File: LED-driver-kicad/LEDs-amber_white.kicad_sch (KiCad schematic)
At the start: 46 parts, among them Q3 2N7002K, Q7 Q_PMOS_GDS, Q8 Q_NMOS_GDS, U7 MIC3205YML-TR

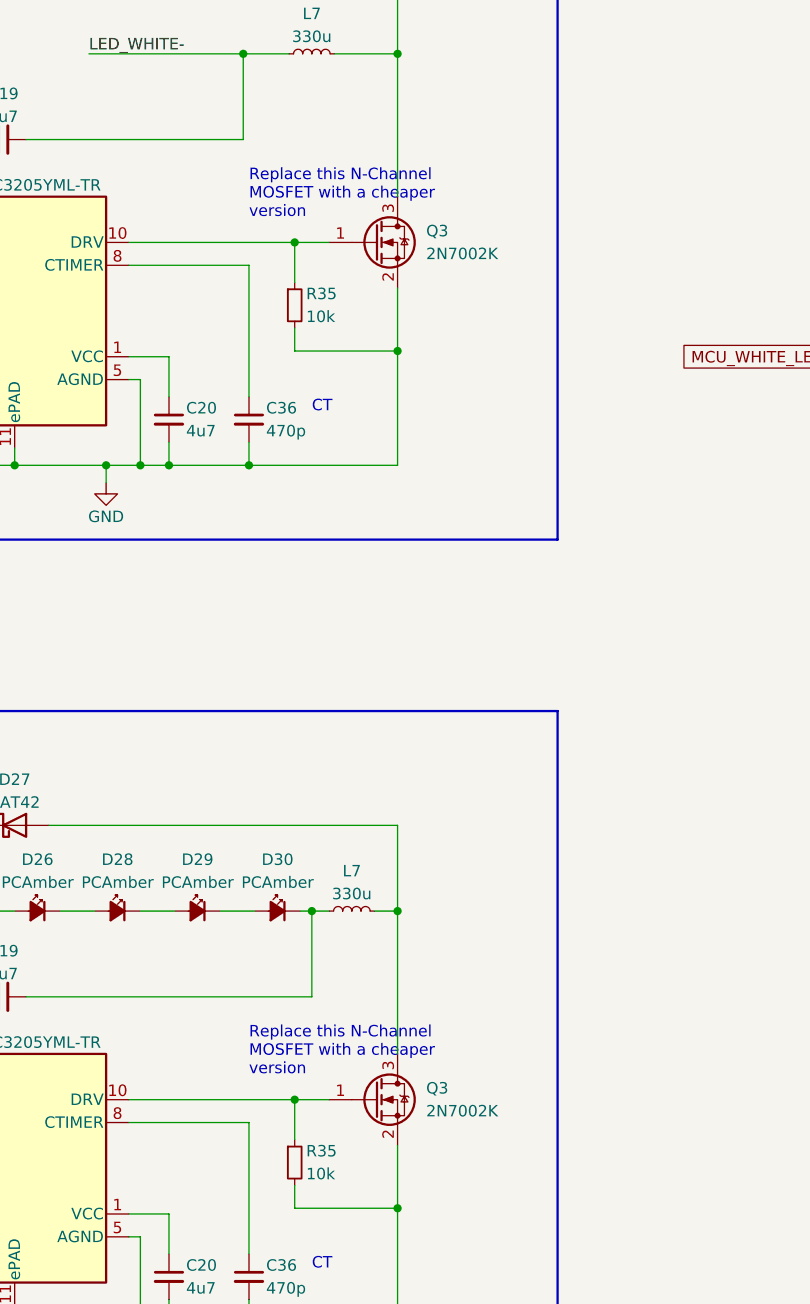
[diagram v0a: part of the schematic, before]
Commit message: replace MOSFETs with generic n-channel MSOFETs
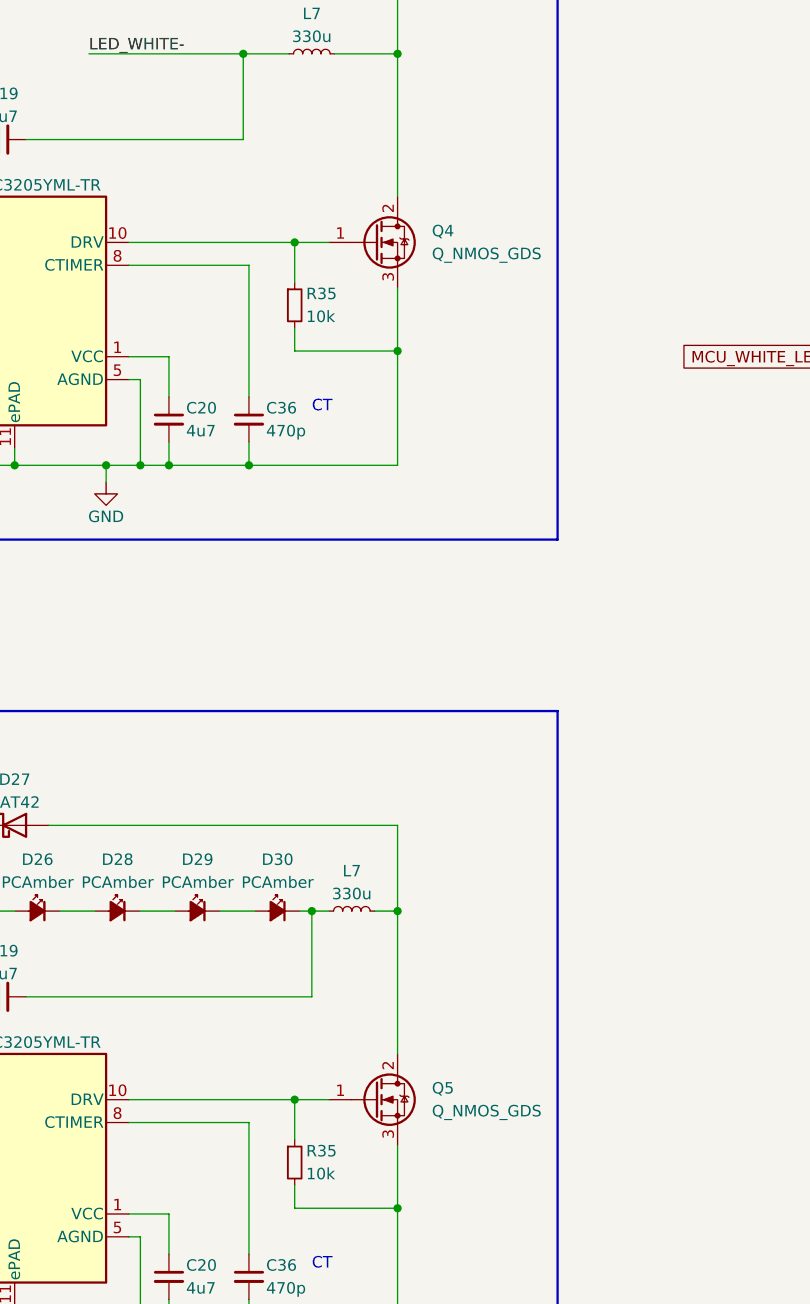
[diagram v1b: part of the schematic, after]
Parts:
- removed Q3 (x2): 2N7002K, Package_TO_SOT_SMD:SOT-23, symbol Transistor_FET:2N7002K
- added Q4, Q5: Q_NMOS_GDS, symbol Device:Q_NMOS_GDS
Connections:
- net GND: now also Q4.3 (S), Q5.3 (S)
- net at D27.2 (A), L7.2: now also Q4.2 (D)
- net at R35.1, U7.10 (DRV): now also Q5.1 (G)
- net at D27.2 (A), L7.2: now also Q5.2 (D)
- net at R35.1, U7.10 (DRV): now also Q4.1 (G)
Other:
- note removed: "Replace this N-Channel MOSFET with a cheaper version"

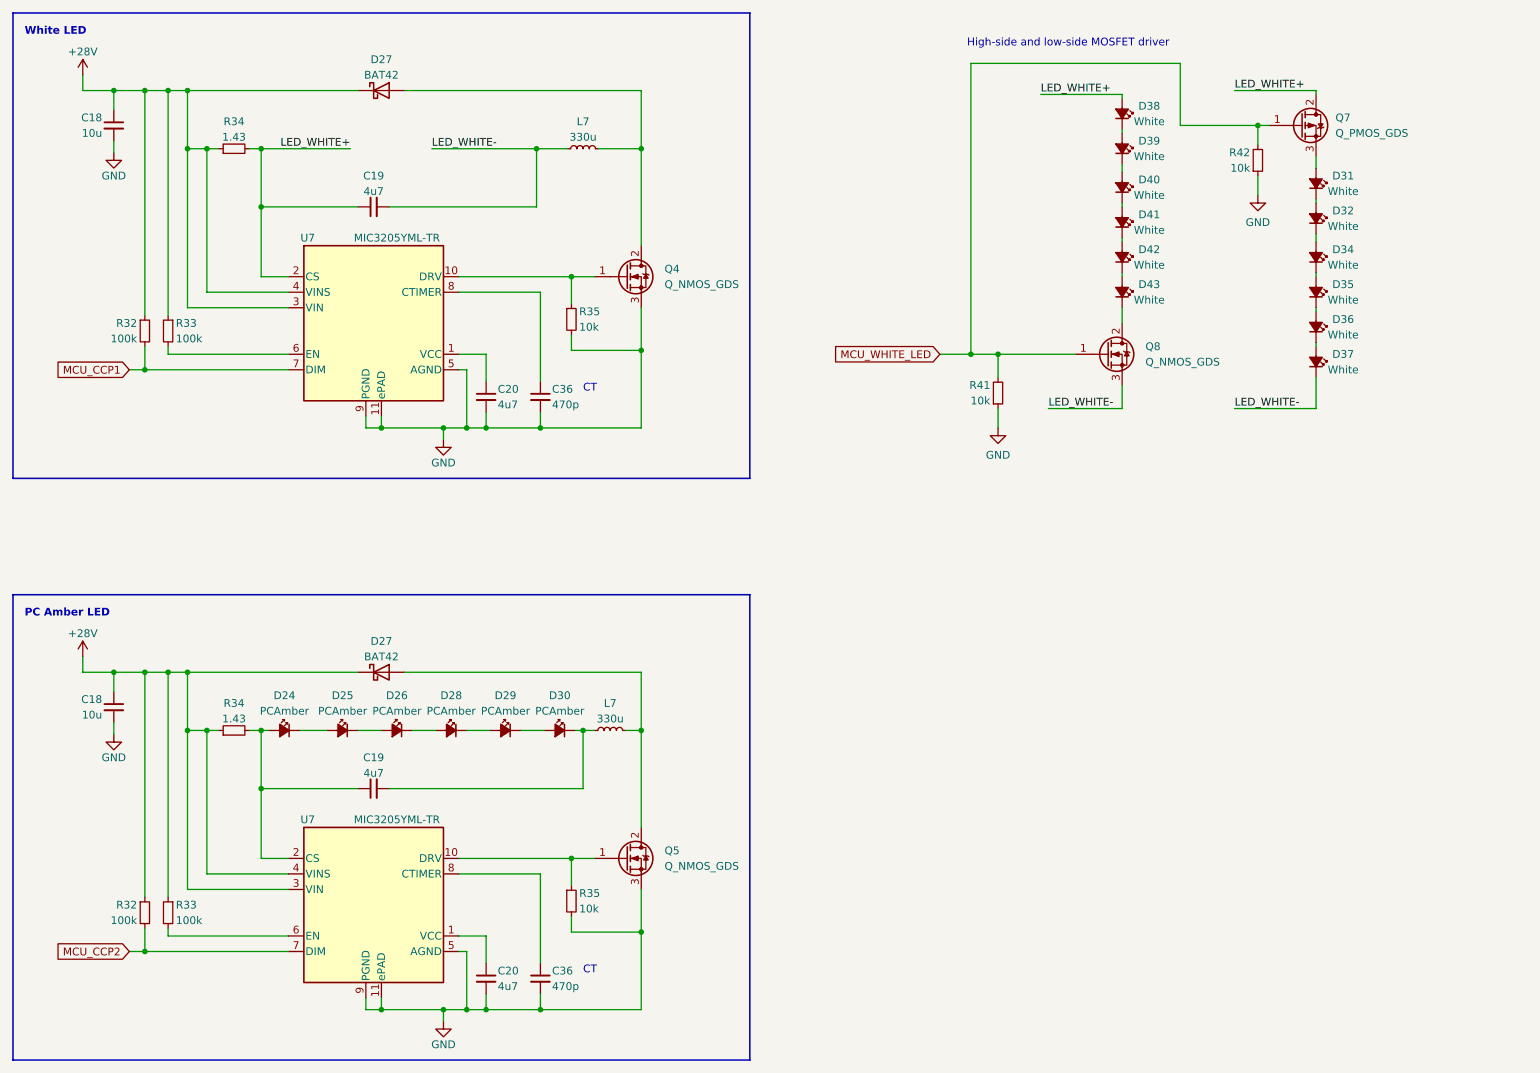
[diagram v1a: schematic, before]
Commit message: replace push-pull MOSFET circuit with LED driver with inverter gate enable
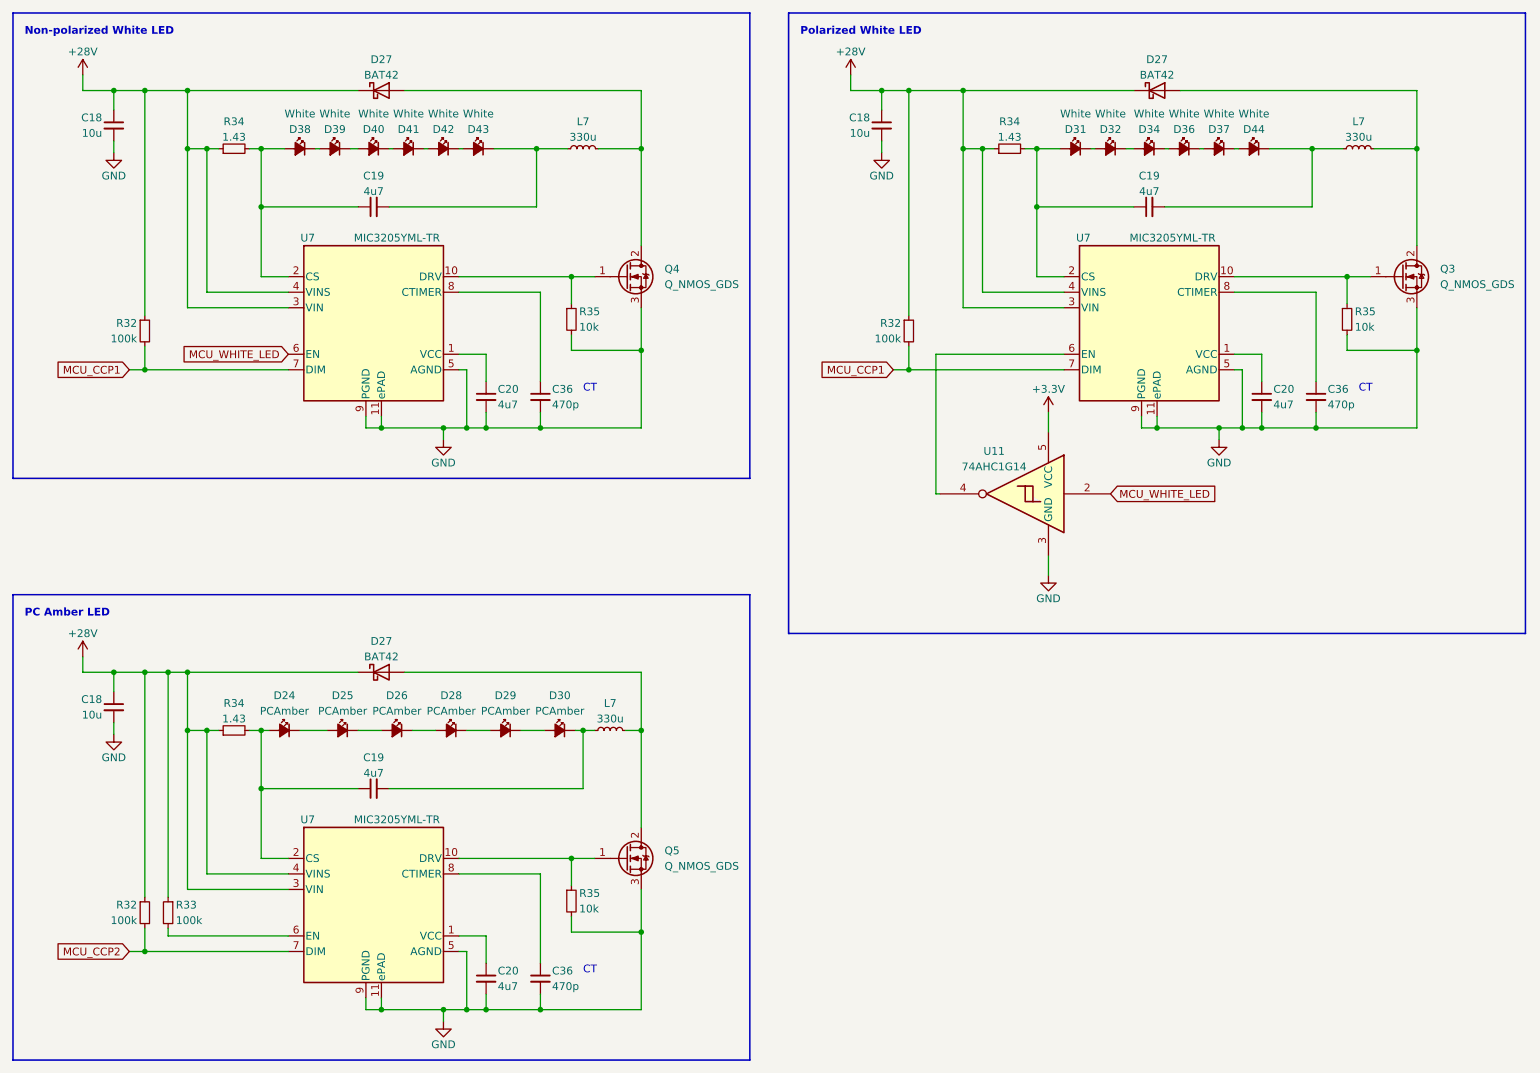
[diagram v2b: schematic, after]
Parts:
- removed D35: White, symbol Device:LED_Small_Filled
- removed Q7: Q_PMOS_GDS, symbol Device:Q_PMOS_GDS
- removed Q8: Q_NMOS_GDS, symbol Device:Q_NMOS_GDS
- removed R33: 100k, symbol Device:R_Small
- removed R41, R42: 10k, symbol Device:R_Small
- added C18: 10u, symbol Device:C_Small
- added C19, C20: 4u7, symbol Device:C_Small
- added C36: 470p, symbol Device:C_Small
- added D27: BAT42, Diode_THT:D_DO-35_SOD27_P7.62mm_Horizontal, symbol Diode:BAT42
- added D44: White, symbol Device:LED_Small_Filled
- added L7: 330u, symbol Device:L_Small
- added Q3: Q_NMOS_GDS, symbol Device:Q_NMOS_GDS
- added R32: 100k, symbol Device:R_Small
- added R34: 1.43, symbol Device:R_Small
- added R35: 10k, symbol Device:R_Small
- added U11: 74AHC1G14, symbol 74xGxx:74AHC1G14
- added U7: MIC3205YML-TR, Mahabeer-Package_DFN_QFN:MLF-10_ML_MCH-Driver_LED_Microchip_MIC3205YML-TR, symbol Driver_LED_Microchip_MIC3205YML-TR:MIC3205YML-TR
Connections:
- net +28V: now also C18.1, D27.1 (K), R32.1, R34.1, U7.3 (VIN), U7.4 (VINS)
- net GND: now also C18.2, C20.2, C36.2, Q3.3 (S), R35.2, U11.3 (GND), U7.11 (ePAD), U7.5 (AGND), U7.9 (PGND)
- net MCU_CCP1: now also R32.2, U7.7 (DIM)
- net MCU_WHITE_LED: now also U7.6 (EN), U11.2
- net at D31.2 (A): now also C19.1, R34.2, U7.2 (CS)
- net at D43.1 (K): now also C19.2, L7.1
- net at D34.1 (K): now also D36.2 (A)
- net LED_WHITE+: no longer names the net of C19.1, D38.2 (A), R34.2, U7.2 (CS)
- removed net LED_WHITE-: C19.2, D37.1 (K), L7.1
- new net: C19.2, D44.1 (K), L7.1
- new net: D37.1 (K), D44.2 (A)
- new net: C36.1, U7.8 (CTIMER)
- new net: Q3.1 (G), R35.1, U7.10 (DRV)
- new net: D27.2 (A), L7.2, Q3.2 (D)
- new net: C20.1, U7.1 (VCC)
- new net: U11.4, U7.6 (EN)
- new net +3.3V: U11.5 (VCC)
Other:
- note added: "Non-polarized White LED"
- note added: "Polarized White LED"
- note removed: "High-side and low-side MOSFET driver"
- note removed: "White LED"
- moved on the sheet: D38, D39, D40, D41, D42, D43

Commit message: update comments and title blocks
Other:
- title: (none) -> Photogrammetry Rig - LED Driver
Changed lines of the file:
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@@
 (kicad_sch (version 20230121) (generator eeschema)
   (paper "A4")
+  (title_block
+    (title "Photogrammetry Rig - LED Driver")
+    (date "2023-08-02")
+    (rev "0.1.0")
+  )
   (junction (at 89.535 86.995) (diameter 0) (color 0 0 0 0)
   )

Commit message: update component designators
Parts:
- renumbered D38 to D33, D39 to D34, D40 to D35, D41 to D36, D42 to D37, D43 to D38, D31 to D39, D32 to D40, D34 to D41, D36 to D42, D37 to D43, Q3 to Q5, Q5 to Q6

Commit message: update footprint assignments
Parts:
- C18: footprint (none) -> Capacitor_SMD:C_1206_3216Metric
- C19, C20: footprint (none) -> Capacitor_SMD:C_0805_2012Metric
- C36: footprint (none) -> Capacitor_SMD:C_0402_1005Metric
- D24, D25, D26, D28, D29, D30: footprint (none) -> LED_SMD:LED_Cree-JE2835_3V_NClass
- D33, D34, D35, D36, D37, D38, D39, D40, D41, D42, D43, D44: footprint (none) -> LED_SMD:LED_Lumiled_Luxeon_2835E_3V
- L7: footprint (none) -> Inductor_SMD:L_1812_4532Metric
- R32, R33, R34, R35: footprint (none) -> Resistor_SMD:R_0402_1005Metric

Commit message: update footprint assignments
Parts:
- D24, D25, D26, D28, D29, D30: footprint LED_SMD:LED_Cree-JE2835_3V_NClass -> KM-LED_SMD:LED_Cree-JE2835_3V_NClass_Group-1
- D33, D34, D35, D36, D37, D38, D39, D40, D41, D42, D43, D44: footprint LED_SMD:LED_Lumiled_Luxeon_2835E_3V -> KM-LED_SMD:LED_Lumiled_Luxeon_2835E_3V
- Q4, Q5, Q6: footprint (none) -> KM-Package_SOT_SMD:SOT-23_Handsoldering
- U11: footprint (none) -> KM-Package_SOT_SMD:SOT-353-DCK5-Logic_Diodes_74AHC1G14SE-7
- U7: footprint Mahabeer-Package_DFN_QFN:MLF-10_ML_MCH-Driver_LED_Microchip_MIC3205YML-TR -> KM-Package_DFN_QFN:MLF-10_ML_MCH-Driver_LED_Microchip_MIC3205YML-TR
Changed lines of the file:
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@@
       (effects (font (size 1.27 1.27)))
     )
-    (property "Footprint" "LED_SMD:LED_Lumiled_Luxeon_2835E_3V" (at 222.25 41.275 90)
+    (property "Footprint" "KM-LED_SMD:LED_Lumiled_Luxeon_2835E_3V" (at 222.25 41.275 90)
       (effects (font (size 1.27 1.27)) hide)
     )
@@
       (effects (font (size 1.27 1.27)))
     )
-    (property "Footprint" "LED_SMD:LED_Lumiled_Luxeon_2835E_3V" (at 198.755 41.275 90)
+    (property "Footprint" "KM-LED_SMD:LED_Lumiled_Luxeon_2835E_3V" (at 198.755 41.275 90)
       (effects (font (size 1.27 1.27)) hide)
     )
@@
       (effects (font (size 1.27 1.27)) (justify left))
     )
-    (property "Footprint" "" (at 251.46 59.69 0)
+    (property "Footprint" "KM-Package_SOT_SMD:SOT-23_Handsoldering" (at 251.46 59.69 0)
       (effects (font (size 1.27 1.27)) hide)
     )
@@
       (effects (font (size 1.27 1.27)))
     )
-    (property "Footprint" "LED_SMD:LED_Lumiled_Luxeon_2835E_3V" (at 95.25 41.275 90)
+    (property "Footprint" "KM-LED_SMD:LED_Lumiled_Luxeon_2835E_3V" (at 95.25 41.275 90)
       (effects (font (size 1.27 1.27)) hide)
     )
@@
       (effects (font (size 1.27 1.27)))
     )
-    (property "Footprint" "LED_SMD:LED_Lumiled_Luxeon_2835E_3V" (at 71.755 41.275 90)
+    (property "Footprint" "KM-LED_SMD:LED_Lumiled_Luxeon_2835E_3V" (at 71.755 41.275 90)
       (effects (font (size 1.27 1.27)) hide)
     )
@@
       (effects (font (size 1.27 1.27)))
     )
-    (property "Footprint" "LED_SMD:LED_Lumiled_Luxeon_2835E_3V" (at 216.535 41.275 90)
+    (property "Footprint" "KM-LED_SMD:LED_Lumiled_Luxeon_2835E_3V" (at 216.535 41.275 90)
       (effects (font (size 1.27 1.27)) hide)
     )
@@
       (effects (font (size 1.27 1.27)))
     )
-    (property "Footprint" "" (at 183.515 97.79 0)
+    (property "Footprint" "KM-Package_SOT_SMD:SOT-353-DCK5-Logic_Diodes_74AHC1G14SE-7" (at 183.515 97.79 0)
       (effects (font (size 1.27 1.27)) hide)
     )
@@
       (effects (font (size 1.27 1.27)))
     )
-    (property "Footprint" "LED_SMD:LED_Cree-JE2835_3V_NClass" (at 108.585 136.525 90)
+    (property "Footprint" "KM-LED_SMD:LED_Cree-JE2835_3V_NClass_Group-1" (at 108.585 136.525 90)
       (effects (font (size 1.27 1.27)) hide)
     )
@@
       (effects (font (size 1.27 1.27)))
     )
-    (property "Footprint" "LED_SMD:LED_Cree-JE2835_3V_NClass" (at 73.025 136.525 90)
+    (property "Footprint" "KM-LED_SMD:LED_Cree-JE2835_3V_NClass_Group-1" (at 73.025 136.525 90)
       (effects (font (size 1.27 1.27)) hide)
     )
@@
       (effects (font (size 1.27 1.27)))
     )
-    (property "Footprint" "LED_SMD:LED_Cree-JE2835_3V_NClass" (at 63.5 136.525 90)
+    (property "Footprint" "KM-LED_SMD:LED_Cree-JE2835_3V_NClass_Group-1" (at 63.5 136.525 90)
       (effects (font (size 1.27 1.27)) hide)
     )
@@
       (effects (font (size 1.27 1.27)))
     )
-    (property "Footprint" "LED_SMD:LED_Cree-JE2835_3V_NClass" (at 90.805 136.525 90)
+    (property "Footprint" "KM-LED_SMD:LED_Cree-JE2835_3V_NClass_Group-1" (at 90.805 136.525 90)
       (effects (font (size 1.27 1.27)) hide)
     )
@@
       (effects (font (size 1.27 1.27)))
     )
-    (property "Footprint" "LED_SMD:LED_Lumiled_Luxeon_2835E_3V" (at 210.82 41.275 90)
+    (property "Footprint" "KM-LED_SMD:LED_Lumiled_Luxeon_2835E_3V" (at 210.82 41.275 90)
       (effects (font (size 1.27 1.27)) hide)
     )
@@
       (effects (font (size 1.27 1.27)))
     )
-    (property "Footprint" "LED_SMD:LED_Lumiled_Luxeon_2835E_3V" (at 89.535 41.275 90)
+    (property "Footprint" "KM-LED_SMD:LED_Lumiled_Luxeon_2835E_3V" (at 89.535 41.275 90)
       (effects (font (size 1.27 1.27)) hide)
     )
@@
       (effects (font (size 1.27 1.27)) (justify left))
     )
-    (property "Footprint" "" (at 124.46 154.94 0)
+    (property "Footprint" "KM-Package_SOT_SMD:SOT-23_Handsoldering" (at 124.46 154.94 0)
       (effects (font (size 1.27 1.27)) hide)
     )
@@
       (effects (font (size 1.27 1.27)))
     )
-    (property "Footprint" "Mahabeer-Package_DFN_QFN:MLF-10_ML_MCH-Driver_LED_Microchip_MIC3205YML-TR" (at 78.105 83.82 0)
+    (property "Footprint" "KM-Package_DFN_QFN:MLF-10_ML_MCH-Driver_LED_Microchip_MIC3205YML-TR" (at 78.105 83.82 0)
       (effects (font (size 1.27 1.27) italic) hide)
     )
@@
       (effects (font (size 1.27 1.27)) (justify left))
     )
-    (property "Footprint" "" (at 124.46 59.69 0)
+    (property "Footprint" "KM-Package_SOT_SMD:SOT-23_Handsoldering" (at 124.46 59.69 0)
       (effects (font (size 1.27 1.27)) hide)
     )
@@
       (effects (font (size 1.27 1.27)))
     )
-    (property "Footprint" "LED_SMD:LED_Lumiled_Luxeon_2835E_3V" (at 66.04 41.275 90)
+    (property "Footprint" "KM-LED_SMD:LED_Lumiled_Luxeon_2835E_3V" (at 66.04 41.275 90)
       (effects (font (size 1.27 1.27)) hide)
     )
@@
       (effects (font (size 1.27 1.27)))
     )
-    (property "Footprint" "LED_SMD:LED_Lumiled_Luxeon_2835E_3V" (at 83.82 41.275 90)
+    (property "Footprint" "KM-LED_SMD:LED_Lumiled_Luxeon_2835E_3V" (at 83.82 41.275 90)
       (effects (font (size 1.27 1.27)) hide)
     )
@@
       (effects (font (size 1.27 1.27)))
     )
-    (property "Footprint" "Mahabeer-Package_DFN_QFN:MLF-10_ML_MCH-Driver_LED_Microchip_MIC3205YML-TR" (at 78.105 179.07 0)
+    (property "Footprint" "KM-Package_DFN_QFN:MLF-10_ML_MCH-Driver_LED_Microchip_MIC3205YML-TR" (at 78.105 179.07 0)
       (effects (font (size 1.27 1.27) italic) hide)
     )
@@
       (effects (font (size 1.27 1.27)))
     )
-    (property "Footprint" "Mahabeer-Package_DFN_QFN:MLF-10_ML_MCH-Driver_LED_Microchip_MIC3205YML-TR" (at 205.105 83.82 0)
+    (property "Footprint" "KM-Package_DFN_QFN:MLF-10_ML_MCH-Driver_LED_Microchip_MIC3205YML-TR" (at 205.105 83.82 0)
       (effects (font (size 1.27 1.27) italic) hide)
     )
@@
       (effects (font (size 1.27 1.27)))
     )
-    (property "Footprint" "LED_SMD:LED_Lumiled_Luxeon_2835E_3V" (at 205.105 41.275 90)
+    (property "Footprint" "KM-LED_SMD:LED_Lumiled_Luxeon_2835E_3V" (at 205.105 41.275 90)
       (effects (font (size 1.27 1.27)) hide)
     )
@@
       (effects (font (size 1.27 1.27)))
     )
-    (property "Footprint" "LED_SMD:LED_Lumiled_Luxeon_2835E_3V" (at 193.04 41.275 90)
+    (property "Footprint" "KM-LED_SMD:LED_Lumiled_Luxeon_2835E_3V" (at 193.04 41.275 90)
       (effects (font (size 1.27 1.27)) hide)
     )
@@
       (effects (font (size 1.27 1.27)))
     )
-    (property "Footprint" "LED_SMD:LED_Cree-JE2835_3V_NClass" (at 81.915 136.525 90)
+    (property "Footprint" "KM-LED_SMD:LED_Cree-JE2835_3V_NClass_Group-1" (at 81.915 136.525 90)
       (effects (font (size 1.27 1.27)) hide)
     )
@@
       (effects (font (size 1.27 1.27)))
     )
-    (property "Footprint" "LED_SMD:LED_Lumiled_Luxeon_2835E_3V" (at 78.105 41.275 90)
+    (property "Footprint" "KM-LED_SMD:LED_Lumiled_Luxeon_2835E_3V" (at 78.105 41.275 90)
       (effects (font (size 1.27 1.27)) hide)
     )
@@
       (effects (font (size 1.27 1.27)))
     )
-    (property "Footprint" "LED_SMD:LED_Cree-JE2835_3V_NClass" (at 99.695 136.525 90)
-      (effects (font (size 1.27 1.27)) hide)
-    )
+    (property "Footprint" "KM-LED_SMD:LED_Cree-JE2835_3V_NClass_Group-1" (at 99.695 136.525 90)
+      (effects (font (size 1.27 1.27)) hide)
+    )
